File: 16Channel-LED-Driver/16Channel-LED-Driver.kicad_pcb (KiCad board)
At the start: 2 copper layers, 190.5 x 80 mm, 241 parts, among them P1 CONN_01X02, P10 CONN_01X02, P11 CONN_01X02, P12 CONN_01X02, P13 CONN_01X02, P14 CONN_01X02, P2 CONN_01X06, P3 CONN_01X02, P4 CONN_01X02, P5 CONN_01X06, P6 CONN_01X08, P7 CONN_01X08, P8 CONN_01X08, P9 CONN_01X08, Q1 Q_NPN_BEC, Q10 Q_NPN_BEC, Q11 BUT11, Q12 Q_NPN_BEC, Q13 BUT11, Q14 Q_NPN_BEC, Q15 Q_NPN_BEC, Q16 Q_NPN_BEC, Q17 BUT11, Q18 Q_NPN_BEC, Q19 Q_NPN_BEC, Q2 Q_NPN_BEC, Q20 Q_NPN_BEC, Q21 BUT11, Q22 Q_NPN_BEC, Q23 BUT11, Q24 Q_NPN_BEC, Q25 BUT11, Q26 Q_NPN_BEC, Q27 Q_NPN_BEC, Q28 Q_NPN_BEC, Q29 Q_NPN_BEC, Q3 Q_NPN_BEC, Q30 Q_NPN_BEC, Q31 BUT11, Q32 Q_NPN_BEC, Q33 BUT11, Q34 Q_NPN_BEC, Q35 Q_NPN_BEC, Q36 BUT11, Q37 Q_NPN_BEC, Q38 BUT11, Q39 Q_NPN_BEC, Q4 Q_NPN_BEC, Q40 Q_NPN_BEC, Q41 Q_NPN_BEC, Q42 Q_NPN_BEC, Q43 Q_NPN_BEC, Q44 Q_NPN_BEC, Q45 Q_NPN_BEC, Q46 Q_NPN_BEC, Q5 BUT11, Q56 BUT11, Q58 BUT11, Q6 Q_NPN_BEC, Q64 BUT11, Q66 BUT11, Q7 BUT11, Q8 Q_NPN_BEC, Q9 Q_NPN_BEC, U1 LD3985G, U2 LD3985G, U3 PCA9634, U4 LM324AN, U5 LM324AN, U6 PCA9634, U7 LM324AN, U8 LM324AN

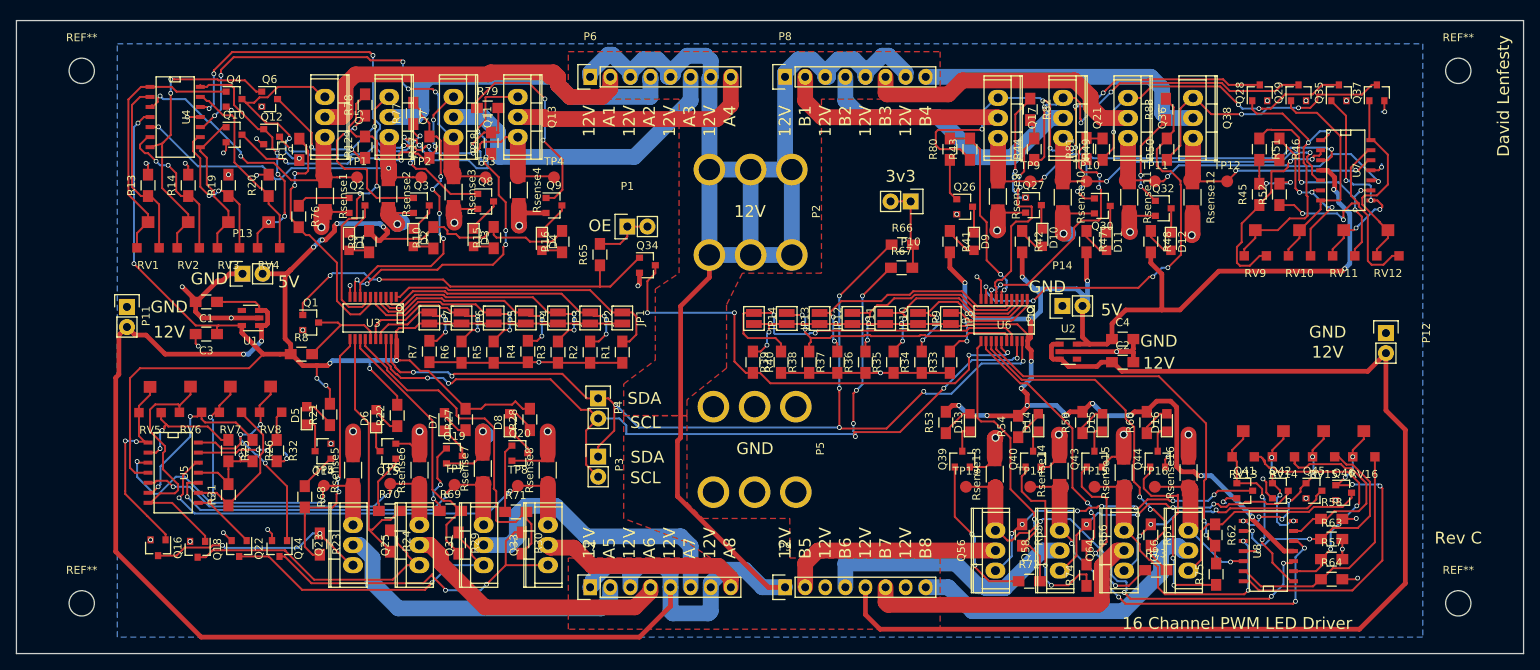
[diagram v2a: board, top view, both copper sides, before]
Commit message: Rev D of the 16 Channel board. Fixed an issue with the opamp driving BJTs
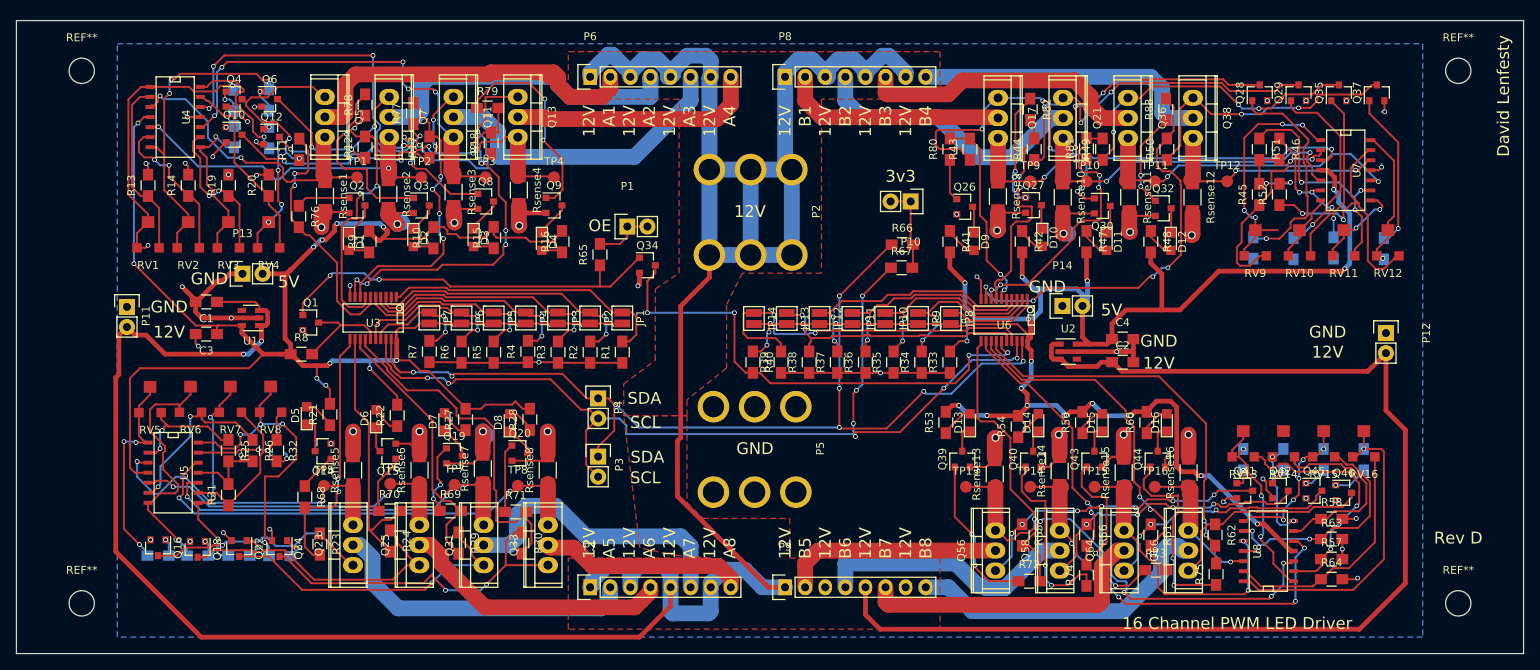
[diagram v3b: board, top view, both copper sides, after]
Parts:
- added R84: 10K, Resistors_SMD:R_0805_HandSoldering, B.Cu at (82.7, 62.2)
- added R85: 10K, Resistors_SMD:R_0805_HandSoldering, B.Cu at (87.2, 62.1)
- added R86: 10K, Resistors_SMD:R_0805_HandSoldering, B.Cu at (82.7, 66.7)
- added R87: 10K, Resistors_SMD:R_0805_HandSoldering, B.Cu at (87.2, 66.9)
- added R88: 10K, Resistors_SMD:R_0805_HandSoldering, B.Cu at (73.2, 119.7)
- added R89: 10K, Resistors_SMD:R_0805_HandSoldering, B.Cu at (78.2, 119.7)
- added R90: 10K, Resistors_SMD:R_0805_HandSoldering, B.Cu at (83.4, 119.7)
- added R91: 10K, Resistors_SMD:R_0805_HandSoldering, B.Cu at (88.5, 119.8)
- added R92: 10K, Resistors_SMD:R_0805_HandSoldering, B.Cu at (211.6, 80.8)
- added R93: 10K, Resistors_SMD:R_0805_HandSoldering, B.Cu at (216.7, 80.9)
- added R94: 10K, Resistors_SMD:R_0805_HandSoldering, B.Cu at (221.7, 80.8)
- added R95: 10K, Resistors_SMD:R_0805_HandSoldering, B.Cu at (228.1, 80.9)
- added R96: 10K, Resistors_SMD:R_0805_HandSoldering, B.Cu at (210.3, 107.6)
- added R97: 10K, Resistors_SMD:R_0805_HandSoldering, B.Cu at (215.4, 107.6)
- added R98: 10K, Resistors_SMD:R_0805_HandSoldering, B.Cu at (220.5, 107.6)
- added R99: 10K, Resistors_SMD:R_0805_HandSoldering, B.Cu at (225.6, 107.6)
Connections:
- RV1 pad 1: Net-(Q4-Pad1) -> Net-(R84-Pad1)
- RV1 pad 2: Net-(Q4-Pad1) -> Net-(R84-Pad1)
- RV10 pad 1: Net-(Q29-Pad1) -> Net-(R93-Pad1)
- RV10 pad 2: Net-(Q29-Pad1) -> Net-(R93-Pad1)
- RV11 pad 1: Net-(Q35-Pad1) -> Net-(R94-Pad1)
- RV11 pad 2: Net-(Q35-Pad1) -> Net-(R94-Pad1)
- RV12 pad 1: Net-(Q37-Pad1) -> Net-(R95-Pad1)
- RV12 pad 2: Net-(Q37-Pad1) -> Net-(R95-Pad1)
- RV13 pad 1: Net-(Q41-Pad1) -> Net-(R96-Pad1)
- RV13 pad 2: Net-(Q41-Pad1) -> Net-(R96-Pad1)
- RV14 pad 1: Net-(Q42-Pad1) -> Net-(R97-Pad1)
- RV14 pad 2: Net-(Q42-Pad1) -> Net-(R97-Pad1)
- RV15 pad 1: Net-(Q45-Pad1) -> Net-(R98-Pad1)
- RV15 pad 2: Net-(Q45-Pad1) -> Net-(R98-Pad1)
- RV16 pad 1: Net-(Q46-Pad1) -> Net-(R99-Pad1)
- RV16 pad 2: Net-(Q46-Pad1) -> Net-(R99-Pad1)
- RV2 pad 1: Net-(Q6-Pad1) -> Net-(R85-Pad1)
- RV2 pad 2: Net-(Q6-Pad1) -> Net-(R85-Pad1)
- RV3 pad 1: Net-(Q10-Pad1) -> Net-(R86-Pad1)
- RV3 pad 2: Net-(Q10-Pad1) -> Net-(R86-Pad1)
- RV4 pad 1: Net-(Q12-Pad1) -> Net-(R87-Pad1)
- RV4 pad 2: Net-(Q12-Pad1) -> Net-(R87-Pad1)
- RV5 pad 1: Net-(Q16-Pad1) -> Net-(R88-Pad1)
- RV5 pad 2: Net-(Q16-Pad1) -> Net-(R88-Pad1)
- RV6 pad 1: Net-(Q18-Pad1) -> Net-(R89-Pad1)
- RV6 pad 2: Net-(Q18-Pad1) -> Net-(R89-Pad1)
- RV7 pad 1: Net-(Q22-Pad1) -> Net-(R90-Pad1)
- RV7 pad 2: Net-(Q22-Pad1) -> Net-(R90-Pad1)
- RV8 pad 1: Net-(Q24-Pad1) -> Net-(R91-Pad1)
- RV8 pad 2: Net-(Q24-Pad1) -> Net-(R91-Pad1)
- RV9 pad 1: Net-(Q28-Pad1) -> Net-(R92-Pad1)
- RV9 pad 2: Net-(Q28-Pad1) -> Net-(R92-Pad1)
- U4 pad 1: Net-(Q4-Pad1) -> Net-(R84-Pad1)
- U4 pad 14: Net-(Q12-Pad1) -> Net-(R87-Pad1)
- U4 pad 7: Net-(Q6-Pad1) -> Net-(R85-Pad1)
- U4 pad 8: Net-(Q10-Pad1) -> Net-(R86-Pad1)
- U5 pad 1: Net-(Q16-Pad1) -> Net-(R88-Pad1)
- U5 pad 14: Net-(Q24-Pad1) -> Net-(R91-Pad1)
- U5 pad 7: Net-(Q18-Pad1) -> Net-(R89-Pad1)
- U5 pad 8: Net-(Q22-Pad1) -> Net-(R90-Pad1)
- U7 pad 1: Net-(Q28-Pad1) -> Net-(R92-Pad1)
- U7 pad 14: Net-(Q37-Pad1) -> Net-(R95-Pad1)
- U7 pad 7: Net-(Q29-Pad1) -> Net-(R93-Pad1)
- U7 pad 8: Net-(Q35-Pad1) -> Net-(R94-Pad1)
- U8 pad 1: Net-(Q41-Pad1) -> Net-(R96-Pad1)
- U8 pad 14: Net-(Q46-Pad1) -> Net-(R99-Pad1)
- U8 pad 7: Net-(Q42-Pad1) -> Net-(R97-Pad1)
- U8 pad 8: Net-(Q45-Pad1) -> Net-(R98-Pad1)
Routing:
- net Net-(R85-Pad1): track 0.00 -> 40.1 mm, vias 0 -> 3
- net Net-(R99-Pad1): track 0.00 -> 40.1 mm, vias 0 -> 1
- net Net-(Q46-Pad1): track 43.6 -> 4.59 mm, vias 4 -> 1
- net Net-(R91-Pad1): track 0.00 -> 38.9 mm, vias 0 -> 4
- net Net-(R84-Pad1): track 0.00 -> 36.6 mm, vias 0 -> 2
- net Net-(Q6-Pad1): track 37.5 -> 2.88 mm, vias 2 -> 1
- net Net-(R89-Pad1): track 0.00 -> 32.9 mm, vias 0 -> 1
- net Net-(Q18-Pad1): track 33.9 -> 1.97 mm, vias 0 -> 1
- net Net-(R87-Pad1): track 0.00 -> 31.8 mm, vias 0 -> 4
- net Net-(R92-Pad1): track 0.00 -> 30.8 mm, vias 0 -> 4
- net Net-(Q4-Pad1): track 33.7 -> 3.33 mm, vias 0 -> 1
- net Net-(Q12-Pad1): track 30.2 -> 0.85 mm, vias 4 -> 1
- net Net-(Q24-Pad1): track 31.8 -> 3.61 mm, vias 3 -> 1
- net Net-(R88-Pad1): track 0.00 -> 27.2 mm, vias 0 -> 3
- net Net-(R90-Pad1): track 0.00 -> 26.7 mm, vias 0 -> 3
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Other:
- board text added: "Rev D"
- board text removed: "Rev C"
